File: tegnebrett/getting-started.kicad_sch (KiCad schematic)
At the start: 55 parts, among them J1 FH12-45S-0.5SH55, J2 FH12-6S-1SH55, J3 Conn_ST_STDC14, J5 MCU_Header_Pin, J8 USB-A1HSW6, SW1 SW_Push, SW2 SW_Push, SW3 SW_Push, SW4 SW_Push, SW5 SW_Push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

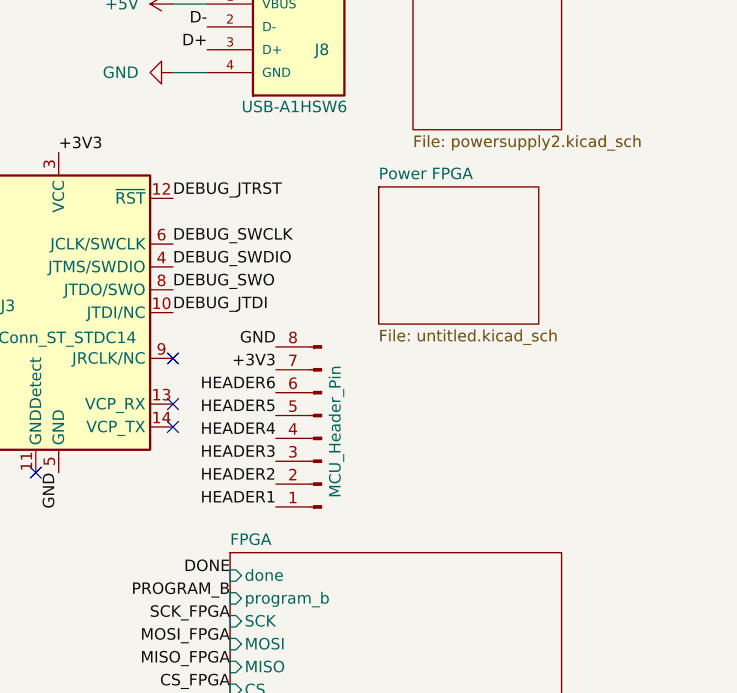
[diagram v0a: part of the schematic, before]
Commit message: feat: add resistors between MCU debug and MCU
These resistors are there in the slides from Asbjørn, so I assume they
should be there. Couldn't find any information on series resistors to
the debug pins in the data sheet. So they may or may not be actually
needed.
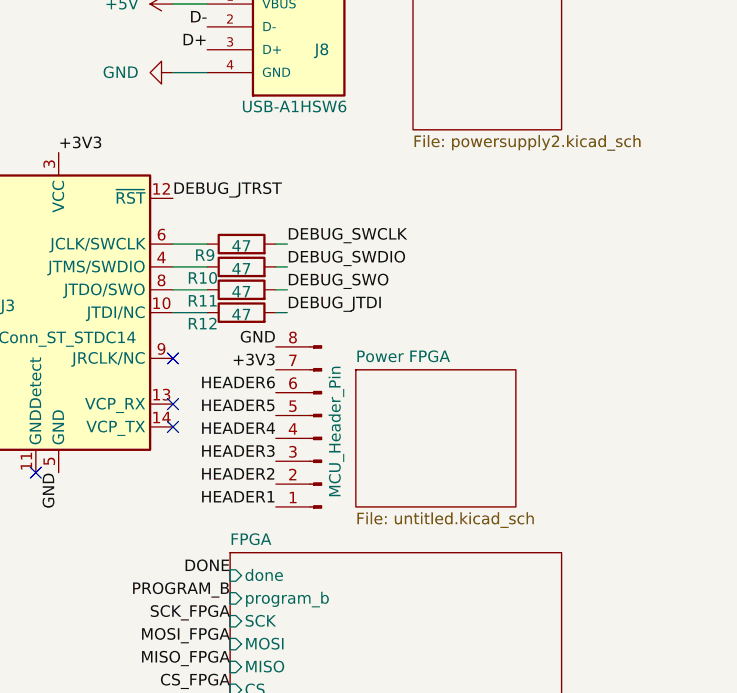
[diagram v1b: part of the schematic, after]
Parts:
- added R10, R11, R12, R9: 47, symbol Device:R
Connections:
- net DEBUG_JTDI: now also R12.2; no longer J3.10 (JTDI/NC)
- net DEBUG_SWCLK: now also R9.2; no longer J3.6 (JCLK/SWCLK)
- net DEBUG_SWDIO: now also R10.2; no longer J3.4 (JTMS/SWDIO)
- net DEBUG_SWO: now also R11.2; no longer J3.8 (JTDO/SWO)
- new net: J3.8 (JTDO/SWO), R11.1
- new net: J3.10 (JTDI/NC), R12.1
- new net: J3.4 (JTMS/SWDIO), R10.1
- new net: J3.6 (JCLK/SWCLK), R9.1

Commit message: feat: add 48MHz crystal footprint + add to PCB
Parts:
- D5, D6, D7, D8, D9: footprint (none) -> tegnebrett_modules:LED_J-SERIES_3030_CRW-M
- Y1: footprint (none) -> tegnebrett_modules:XRCGB48M000F4M00R0_MUR
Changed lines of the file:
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@@
 			)
 		)
-		(property "Footprint" ""
+		(property "Footprint" "tegnebrett_modules:LED_J-SERIES_3030_CRW-M"
 			(at 179.07 76.2 0)
 			(effects
@@
 			)
 		)
-		(property "Footprint" ""
+		(property "Footprint" "tegnebrett_modules:LED_J-SERIES_3030_CRW-M"
 			(at 157.48 96.52 0)
 			(effects
@@
 			)
 		)
-		(property "Footprint" ""
+		(property "Footprint" "tegnebrett_modules:LED_J-SERIES_3030_CRW-M"
 			(at 157.48 78.74 0)
 			(effects
@@
 			)
 		)
-		(property "Footprint" ""
+		(property "Footprint" "tegnebrett_modules:LED_J-SERIES_3030_CRW-M"
 			(at 157.48 73.66 0)
 			(effects
@@
 			)
 		)
-		(property "Footprint" ""
+		(property "Footprint" "tegnebrett_modules:XRCGB48M000F4M00R0_MUR"
 			(at 53.34 72.39 0)
 			(effects
@@
 			)
 		)
-		(property "Footprint" ""
+		(property "Footprint" "tegnebrett_modules:LED_J-SERIES_3030_CRW-M"
 			(at 179.07 99.06 0)
 			(effects

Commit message: feat: add footprint for each capacitor
It's all 0805, 1206 or 1210 hand soldering variants.
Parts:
- C71, C72, C73, C74, C75, C76, C77, C78, C80, C81, C82, C84, C85, C86: footprint (none) -> Capacitor_SMD:C_0805_2012Metric_Pad1.18x1.45mm_HandSolder
- C79, C83: footprint (none) -> Capacitor_SMD:C_1206_3216Metric_Pad1.33x1.80mm_HandSolder
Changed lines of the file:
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@@
 			)
 		)
-		(property "Footprint" ""
+		(property "Footprint" "Capacitor_SMD:C_0805_2012Metric_Pad1.18x1.45mm_HandSolder"
 			(at 277.8252 26.67 0)
 			(effects
@@
 			)
 		)
-		(property "Footprint" ""
+		(property "Footprint" "Capacitor_SMD:C_0805_2012Metric_Pad1.18x1.45mm_HandSolder"
 			(at 220.6752 27.94 0)
 			(effects
@@
 			)
 		)
-		(property "Footprint" ""
+		(property "Footprint" "Capacitor_SMD:C_0805_2012Metric_Pad1.18x1.45mm_HandSolder"
 			(at 265.1252 26.67 0)
 			(effects
@@
 			)
 		)
-		(property "Footprint" ""
+		(property "Footprint" "Capacitor_SMD:C_0805_2012Metric_Pad1.18x1.45mm_HandSolder"
 			(at 47.9552 86.36 0)
 			(effects
@@
 			)
 		)
-		(property "Footprint" ""
+		(property "Footprint" "Capacitor_SMD:C_0805_2012Metric_Pad1.18x1.45mm_HandSolder"
 			(at 60.6552 86.36 0)
 			(effects
@@
 			)
 		)
-		(property "Footprint" ""
+		(property "Footprint" "Capacitor_SMD:C_0805_2012Metric_Pad1.18x1.45mm_HandSolder"
 			(at 242.2652 58.42 0)
 			(effects
@@
 			)
 		)
-		(property "Footprint" ""
+		(property "Footprint" "Capacitor_SMD:C_0805_2012Metric_Pad1.18x1.45mm_HandSolder"
 			(at 187.6552 27.94 0)
 			(effects
@@
 			)
 		)
-		(property "Footprint" ""
+		(property "Footprint" "Capacitor_SMD:C_0805_2012Metric_Pad1.18x1.45mm_HandSolder"
 			(at 134.62 34.5948 0)
 			(effects
@@
 			)
 		)
-		(property "Footprint" ""
+		(property "Footprint" "Capacitor_SMD:C_0805_2012Metric_Pad1.18x1.45mm_HandSolder"
 			(at 76.2 59.9948 0)
 			(effects
@@
 			)
 		)
-		(property "Footprint" ""
+		(property "Footprint" "Capacitor_SMD:C_0805_2012Metric_Pad1.18x1.45mm_HandSolder"
 			(at 197.8152 27.94 0)
 			(effects
@@
 			)
 		)
-		(property "Footprint" ""
+		(property "Footprint" "Capacitor_SMD:C_0805_2012Metric_Pad1.18x1.45mm_HandSolder"
 			(at 232.1052 27.94 0)
 			(effects
@@
 			)
 		)
-		(property "Footprint" ""
+		(property "Footprint" "Capacitor_SMD:C_1206_3216Metric_Pad1.33x1.80mm_HandSolder"
 			(at 197.8152 53.34 0)
 			(effects
@@
 			)
 		)
-		(property "Footprint" ""
+		(property "Footprint" "Capacitor_SMD:C_0805_2012Metric_Pad1.18x1.45mm_HandSolder"
 			(at 80.3148 40.64 0)
 			(effects
@@
 			)
 		)
-		(property "Footprint" ""
+		(property "Footprint" "Capacitor_SMD:C_0805_2012Metric_Pad1.18x1.45mm_HandSolder"
 			(at 209.2452 27.94 0)
 			(effects
@@
 			)
 		)
-		(property "Footprint" ""
+		(property "Footprint" "Capacitor_SMD:C_1206_3216Metric_Pad1.33x1.80mm_HandSolder"
 			(at 244.8052 27.94 0)
 			(effects
@@
 			)
 		)
-		(property "Footprint" ""
+		(property "Footprint" "Capacitor_SMD:C_0805_2012Metric_Pad1.18x1.45mm_HandSolder"
 			(at 229.5652 58.42 0)
 			(effects

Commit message: feat: add footprints to inductors
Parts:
- L4: footprint (none) -> Inductor_SMD:L_0805_2012Metric_Pad1.15x1.40mm_HandSolder
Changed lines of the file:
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@@
 			)
 		)
-		(property "Footprint" ""
+		(property "Footprint" "Inductor_SMD:L_0805_2012Metric_Pad1.15x1.40mm_HandSolder"
 			(at 228.6 44.45 0)
 			(effects

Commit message: feat: add footprint to resistors
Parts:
- R10, R11, R12, R17, R18, R19, R20, R21, R63, R65, R66, R67, R68, R69, R70, R9: footprint (none) -> Resistor_SMD:R_0805_2012Metric_Pad1.20x1.40mm_HandSolder
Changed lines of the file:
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@@
 			)
 		)
-		(property "Footprint" ""
+		(property "Footprint" "Resistor_SMD:R_0805_2012Metric_Pad1.20x1.40mm_HandSolder"
 			(at 165.608 158.75 90)
 			(effects
@@
 			)
 		)
-		(property "Footprint" ""
+		(property "Footprint" "Resistor_SMD:R_0805_2012Metric_Pad1.20x1.40mm_HandSolder"
 			(at 247.65 102.108 90)
 			(effects
@@
 			)
 		)
-		(property "Footprint" ""
+		(property "Footprint" "Resistor_SMD:R_0805_2012Metric_Pad1.20x1.40mm_HandSolder"
 			(at 59.182 172.72 90)
 			(effects
@@
 			)
 		)
-		(property "Footprint" ""
+		(property "Footprint" "Resistor_SMD:R_0805_2012Metric_Pad1.20x1.40mm_HandSolder"
 			(at 155.448 173.99 90)
 			(effects
@@
 			)
 		)
-		(property "Footprint" ""
+		(property "Footprint" "Resistor_SMD:R_0805_2012Metric_Pad1.20x1.40mm_HandSolder"
 			(at 160.782 140.97 90)
 			(effects
@@
 			)
 		)
-		(property "Footprint" ""
+		(property "Footprint" "Resistor_SMD:R_0805_2012Metric_Pad1.20x1.40mm_HandSolder"
 			(at 46.482 172.72 90)
 			(effects
@@
 			)
 		)
-		(property "Footprint" ""
+		(property "Footprint" "Resistor_SMD:R_0805_2012Metric_Pad1.20x1.40mm_HandSolder"
 			(at 210.058 157.48 90)
 			(effects
@@
 			)
 		)
-		(property "Footprint" ""
+		(property "Footprint" "Resistor_SMD:R_0805_2012Metric_Pad1.20x1.40mm_HandSolder"
 			(at 189.738 157.48 90)
 			(effects
@@
 			)
 		)
-		(property "Footprint" ""
+		(property "Footprint" "Resistor_SMD:R_0805_2012Metric_Pad1.20x1.40mm_HandSolder"
 			(at 247.65 104.648 90)
 			(effects
@@
 			)
 		)
-		(property "Footprint" ""
+		(property "Footprint" "Resistor_SMD:R_0805_2012Metric_Pad1.20x1.40mm_HandSolder"
 			(at 163.322 125.73 90)
 			(effects
@@
 			)
 		)
-		(property "Footprint" ""
+		(property "Footprint" "Resistor_SMD:R_0805_2012Metric_Pad1.20x1.40mm_HandSolder"
 			(at 52.832 172.72 90)
 			(effects
@@
 			)
 		)
-		(property "Footprint" ""
+		(property "Footprint" "Resistor_SMD:R_0805_2012Metric_Pad1.20x1.40mm_HandSolder"
 			(at 247.65 99.568 90)
 			(effects
@@
 			)
 		)
-		(property "Footprint" ""
+		(property "Footprint" "Resistor_SMD:R_0805_2012Metric_Pad1.20x1.40mm_HandSolder"
 			(at 40.132 172.72 90)
 			(effects
@@
 			)
 		)
-		(property "Footprint" ""
+		(property "Footprint" "Resistor_SMD:R_0805_2012Metric_Pad1.20x1.40mm_HandSolder"
 			(at 183.388 137.16 90)
 			(effects
@@
 			)
 		)
-		(property "Footprint" ""
+		(property "Footprint" "Resistor_SMD:R_0805_2012Metric_Pad1.20x1.40mm_HandSolder"
 			(at 46.482 31.75 90)
 			(effects
@@
 			)
 		)
-		(property "Footprint" ""
+		(property "Footprint" "Resistor_SMD:R_0805_2012Metric_Pad1.20x1.40mm_HandSolder"
 			(at 247.65 97.028 90)
 			(effects

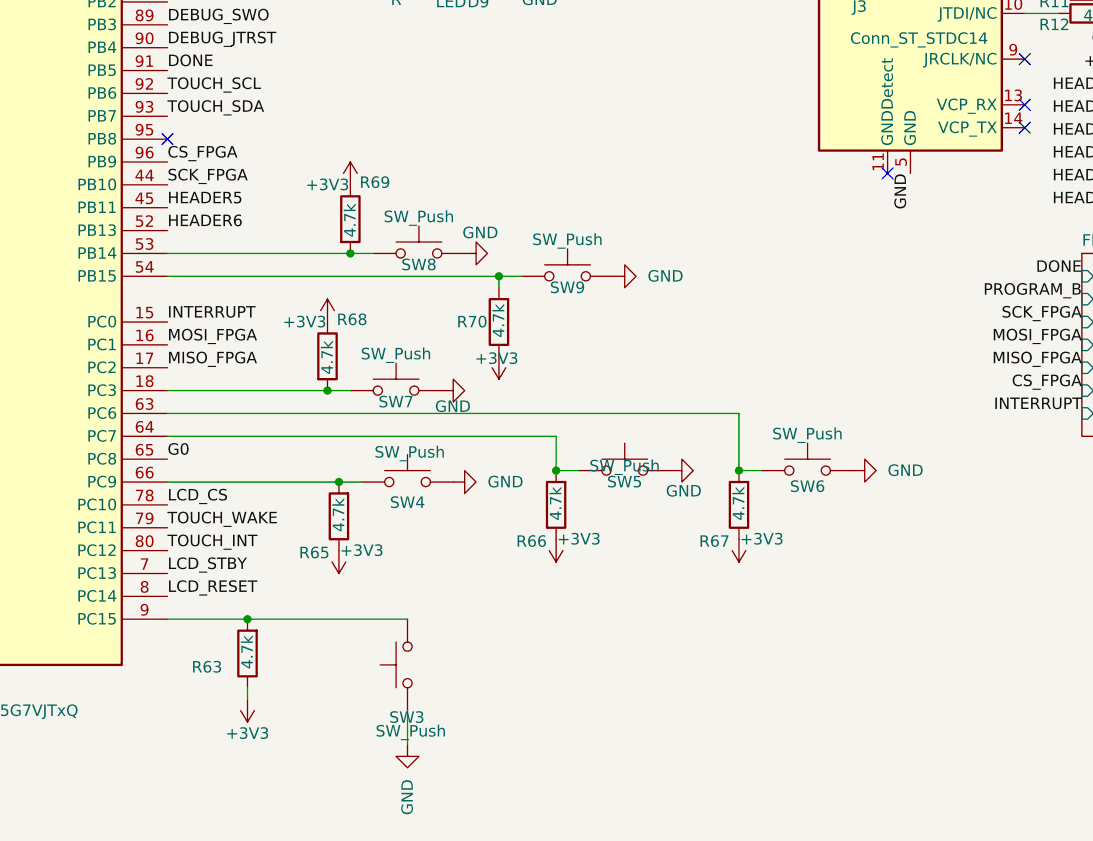
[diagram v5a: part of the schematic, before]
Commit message: refactor: remove some general bottuns from MCU
We have gone down from 9 buttons total to 6 buttons total.
One button is connected to the FPGA.
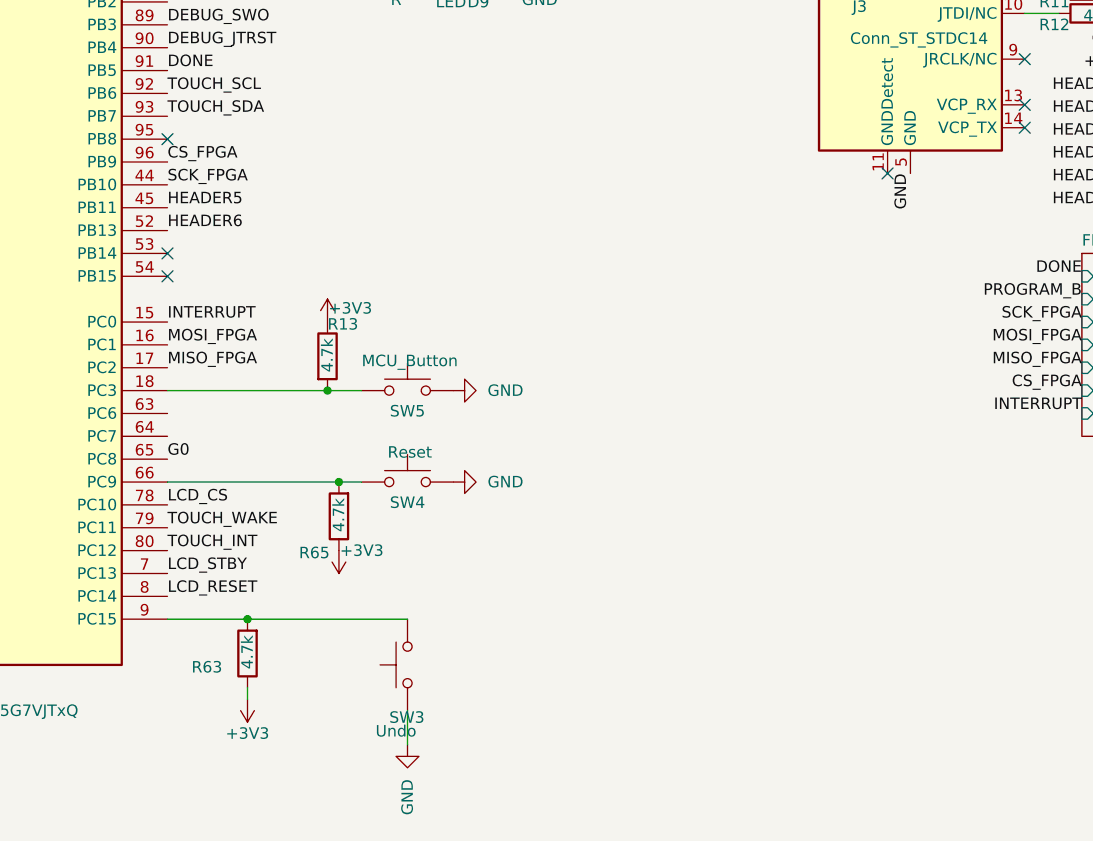
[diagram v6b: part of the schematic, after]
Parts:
- removed R66, R67, R68, R69, R70: 4.7k, Resistor_SMD:R_0805_2012Metric_Pad1.20x1.40mm_HandSolder, symbol Device:R
- removed SW6, SW7, SW8, SW9: SW_Push, symbol Switch:SW_Push
- added R13: 4.7k, Resistor_SMD:R_0805_2012Metric_Pad1.20x1.40mm_HandSolder, symbol Device:R
- SW3: value SW_Push -> Undo
- SW4: value SW_Push -> Reset
- SW5: value SW_Push -> MCU_Button
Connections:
- net +3V3: now also R13.1
- net at SW5.1: now also U5.18 (PC3), R13.2; no longer U5.64 (PC7)
- no-connect marks 12 -> 14

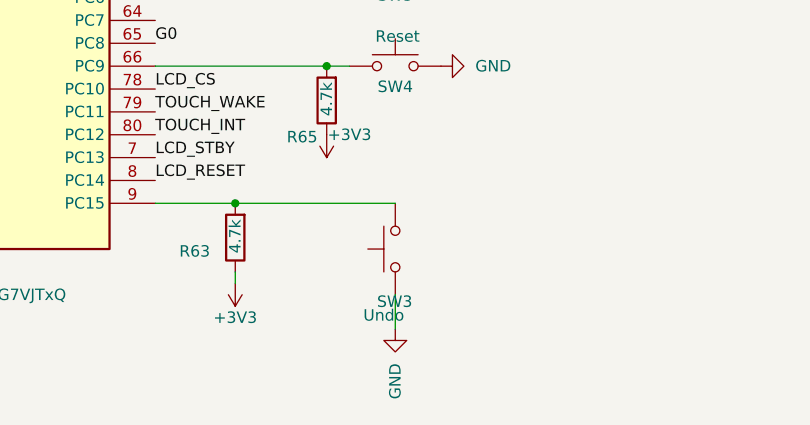
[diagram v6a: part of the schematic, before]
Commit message: feat: import and add footprints for GamePlay buttons undo and reset
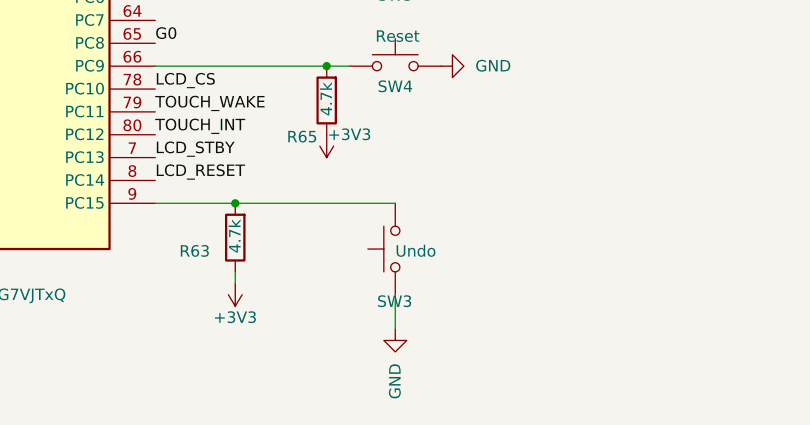
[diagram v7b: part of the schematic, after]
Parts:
- SW3, SW4: footprint (none) -> tegnebrett_modules:SW_KS11R23CQD
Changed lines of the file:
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@@
 			)
 		)
-		(property "Footprint" ""
+		(property "Footprint" "tegnebrett_modules:SW_KS11R23CQD"
 			(at 171.45 149.86 0)
 			(effects
@@
 		)
 		(property "Value" "Undo"
-			(at 167.894 182.626 90)
+			(at 171.45 175.514 90)
 			(effects
 				(font
@@
 			)
 		)
-		(property "Footprint" ""
+		(property "Footprint" "tegnebrett_modules:SW_KS11R23CQD"
 			(at 166.37 175.26 0)
 			(effects

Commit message: feat: add and import footprints of trash buttons
These buttons are cheap and do the job fine.
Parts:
- SW1, SW2, SW5: footprint (none) -> tegnebrett_modules:SW_PS1024ALRED
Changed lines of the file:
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@@
 			)
 		)
-		(property "Footprint" ""
+		(property "Footprint" "tegnebrett_modules:SW_PS1024ALRED"
 			(at 71.12 44.45 0)
 			(effects
@@
 			)
 		)
-		(property "Footprint" ""
+		(property "Footprint" "tegnebrett_modules:SW_PS1024ALRED"
 			(at 55.88 33.02 0)
 			(effects
@@
 			)
 		)
-		(property "Footprint" ""
+		(property "Footprint" "tegnebrett_modules:SW_PS1024ALRED"
 			(at 171.45 139.7 0)
 			(effects
